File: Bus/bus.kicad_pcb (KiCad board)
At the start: 4 copper layers, 69.3 x 213.7 mm, 38 parts, among them J1 Conn_01x05_Pin, J10 USB_C_Receptacle_PowerOnly_6P, J11 Conn_01x10_Pin, J12 Conn_01x05_Pin, J2 Conn_01x08_Pin, J3 Conn_01x06_Pin, J4 Conn_01x08_Pin, J5 Conn_01x06_Pin, J6 Conn_01x08_Pin, J7 Conn_01x06_Pin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

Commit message: Added pins to bus PCB. Oh boy it's going to be long
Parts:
- added J10: Conn_01x10_Pin, Connector_PinHeader_2.54mm:PinHeader_1x10_P2.54mm_Vertical, F.Cu at (159.8, 28.4)
- added J13: Conn_01x08_Pin, Connector_PinHeader_2.54mm:PinHeader_1x08_P2.54mm_Vertical, F.Cu at (100.3, 173.7)
- added J14: Conn_01x08_Pin, Connector_PinHeader_2.54mm:PinHeader_1x08_P2.54mm_Vertical, F.Cu at (100.6, 196.1)
- added J15: Conn_01x06_Pin, Connector_PinHeader_2.54mm:PinHeader_1x06_P2.54mm_Vertical, F.Cu at (100.6, 48.3)
- added J16: Conn_01x03_Pin, Connector_PinHeader_2.54mm:PinHeader_1x03_P2.54mm_Vertical, F.Cu at (100.6, 65.3)
- added J17: Conn_01x10_Pin, Connector_PinHeader_2.54mm:PinHeader_1x10_P2.54mm_Vertical, F.Cu at (100.6, 75.4)
- added J18: Conn_01x03_Pin, Connector_PinHeader_2.54mm:PinHeader_1x03_P2.54mm_Vertical, F.Cu at (100.7, 102.6)
- added J19: Conn_01x10_Pin, Connector_PinHeader_2.54mm:PinHeader_1x10_P2.54mm_Vertical, F.Cu at (160.3, 241.0)
- added J20: Conn_01x03_Pin, Connector_PinHeader_2.54mm:PinHeader_1x03_P2.54mm_Vertical, F.Cu at (160.5, 268.2)
- added J21: Conn_01x10_Pin, Connector_PinHeader_2.54mm:PinHeader_1x10_P2.54mm_Vertical, F.Cu at (160.3, 200.2)
- added J22: Conn_01x04_Pin, Connector_PinHeader_2.54mm:PinHeader_1x04_P2.54mm_Vertical, F.Cu at (160.3, 227.8)
- J11: value Conn_01x10_Pin -> Conn_01x05_Pin; footprint Connector_PinHeader_2.54mm:PinHeader_1x10_P2.54mm_Vertical -> Connector_PinHeader_2.54mm:PinHeader_1x05_P2.54mm_Vertical
- J12: value Conn_01x05_Pin -> Conn_01x07_Pin; footprint Connector_PinHeader_2.54mm:PinHeader_1x05_P2.54mm_Vertical -> Connector_PinHeader_2.54mm:PinHeader_1x07_P2.54mm_Vertical
- J2, J4, J6: value Conn_01x08_Pin -> Conn_01x10_Pin; footprint Connector_PinHeader_2.54mm:PinHeader_1x08_P2.54mm_Vertical -> Connector_PinHeader_2.54mm:PinHeader_1x10_P2.54mm_Vertical
- J3, J5, J7: value Conn_01x06_Pin -> Conn_01x04_Pin; footprint Connector_PinHeader_2.54mm:PinHeader_1x06_P2.54mm_Vertical -> Connector_PinHeader_2.54mm:PinHeader_1x04_P2.54mm_Vertical
- J9: value Conn_01x06_Pin -> Conn_01x07_Pin; footprint Connector_PinHeader_2.54mm:PinHeader_1x06_P2.54mm_Vertical -> Connector_PinHeader_2.54mm:PinHeader_1x07_P2.54mm_Vertical
- moved J12 128.9 mm to (100.8, 153.2)
- moved J5 77.4 mm to (160.3, 187.7)
- moved J7 77.1 mm to (100.6, 140.0)
- moved J9 55.0 mm to (160.0, 139.2)
- moved J6 51.4 mm to (100.6, 113.3)
- moved J4 48.2 mm to (160.0, 160.0)
- moved J3 39.7 mm to (160.0, 99.6)
- moved J8 28.8 mm to (160.2, 112.0)
- moved J11 22.7 mm to (159.8, 55.9)
- moved J1 13.0 mm to (100.6, 29.0)
- moved J2 10.7 mm to (159.9, 71.9)
- renumbered J10 to J23
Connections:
- J1 pad 4: /~CLK -> /~{CLK}
- J1 pad 5: /Halt -> /HALT
- J11 pad 1: +5V -> /PC_~{JMP}
- J11 pad 2: GND -> /PC_CE
- J11 pad 3: /B7 -> /CLK
- J11 pad 4: /B6 -> /~RST
- J11 pad 5: /B5 -> /PC_~{CO}
- J12 pad 1: /PC ~CO -> +5V
- J12 pad 2: /~RST -> GND
- J12 pad 3: /CLK -> /ALU_CARRY
- J12 pad 4: /PC CE -> /ALU_ZERO
- J12 pad 5: /PC ~JMP -> /~{CLK}
- J2 pad 1: /B7 -> +5V
- J2 pad 2: /B6 -> GND
- J2 pad 3: /B5 -> /B0
- J2 pad 4: /B4 -> /B1
- J2 pad 5: /B3 -> /B2
- J2 pad 6: /B2 -> /B3
- J2 pad 7: /B1 -> /B4
- J2 pad 8: /B0 -> /B5
- J3 pad 1: /ARegister/~Write -> /AR_~{WRITE}
- J3 pad 3: /ARegister/~Read -> /AR_~{READ}
- J4 pad 1: /B7 -> +5V
- J4 pad 2: /B6 -> GND
- J4 pad 3: /B5 -> /B0
- J4 pad 4: /B4 -> /B1
- J4 pad 5: /B3 -> /B2
- J4 pad 6: /B2 -> /B3
- J4 pad 7: /B1 -> /B4
- J4 pad 8: /B0 -> /B5
- J5 pad 3: /BRegister/~Read -> /BR_~{READ}
- J6 pad 1: /B7 -> +5V
- J6 pad 2: /B6 -> GND
- J6 pad 3: /B5 -> /B0
- J6 pad 4: /B4 -> /B1
- J6 pad 5: /InstructionRegister/B3 -> /B2
- J6 pad 6: /InstructionRegister/B2 -> /B3
- J6 pad 7: /InstructionRegister/B1 -> /B4
- J6 pad 8: /InstructionRegister/B0 -> /B5
- J7 pad 1: /InstructionRegister/~Write -> /CLK
- J7 pad 2: /RST -> /IR_~{READ}
- J7 pad 3: /InstructionRegister/~Read -> /RST
- J7 pad 4: /CLK -> /IR_~{WRITE}
- J9 pad 1: /ALU/~Write -> /ALU_~{WRITE}
- J9 pad 2: /ALU/Sub -> /ALU_SUB
- J9 pad 5: /ALU/Carry flag -> /ALU_FI
- J9 pad 6: /ALU/Zero flag -> /ALU_CARRY
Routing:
- net (no net): track 0.00 -> 447.7 mm
- net /PC_~{JMP}: track 0.00 -> 107.8 mm
- net /PC ~CO: track 107.8 -> 0.00 mm
- net /~RST: track 160.5 -> 260.5 mm
- net /PC CE: track 99.9 -> 0.00 mm
- net /PC_~{CO}: track 0.00 -> 97.1 mm
- net /PC ~JMP: track 97.1 -> 0.00 mm
- net /~CLK: track 91.0 -> 0.00 mm, vias 1 -> 0
- net /MAR_~{EN}: track 0.00 -> 91.0 mm, vias 0 -> 1
- net /ARegister/~Write: track 81.2 -> 0.00 mm
- net /Halt: track 76.2 -> 0.00 mm
- net /HALT: track 0.00 -> 76.2 mm
- net /ARegister/~Read: track 75.9 -> 0.00 mm
- net /InstructionRegister/~Write: track 62.7 -> 0.00 mm
- net /InstructionRegister/~Read: track 57.4 -> 0.00 mm
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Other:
- board size 69.3 x 213.7 mm -> 69.3 x 273.9 mm

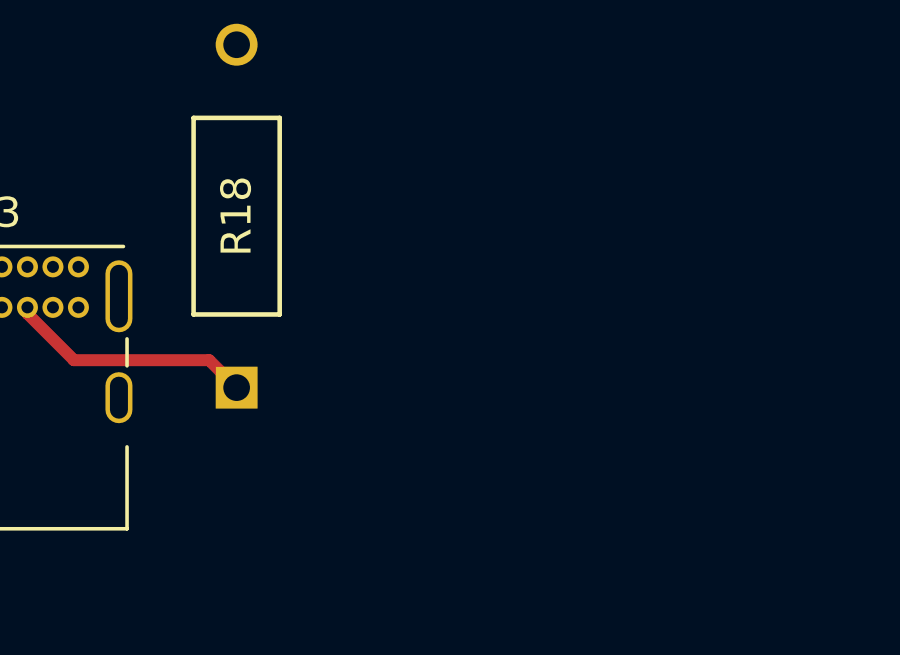
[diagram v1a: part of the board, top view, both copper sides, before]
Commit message: Added an extra power option if I can't solder the USB header
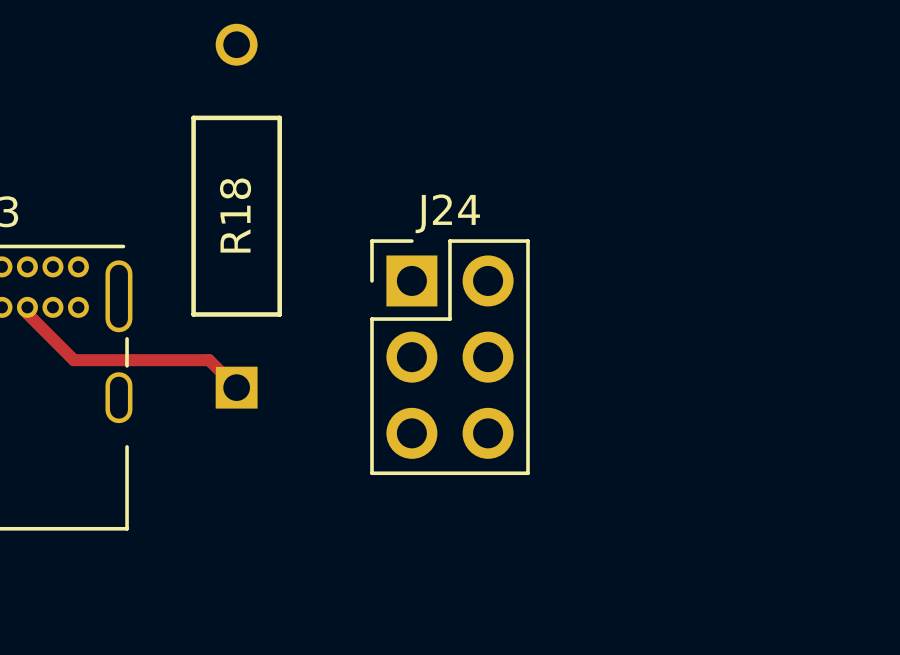
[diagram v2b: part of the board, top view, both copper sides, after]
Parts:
- added J24: Conn_02x03_Counter_Clockwise, Connector_PinHeader_2.54mm:PinHeader_2x03_P2.54mm_Vertical, F.Cu at (139.2, 184.7)

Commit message: Aligned bus pins with where they will fit when connected to the other modules
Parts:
- moved R17 85.7 mm to (109.2, 262.1), turned to 90 degrees
- moved J23 82.5 mm to (107.8, 265.4)
- moved J24 81.6 mm to (118.9, 263.7)
- moved R1 81.1 mm to (120.7, 243.8)
- moved R3 81.1 mm to (127.3, 243.8)
- moved R4 81.1 mm to (130.6, 243.8)
- moved R5 81.1 mm to (133.9, 243.8)
- moved R8 81.1 mm to (143.8, 243.8)
- moved R2 81.1 mm to (124.0, 243.8)
- moved R6 81.1 mm to (137.2, 243.8)
- moved R7 81.1 mm to (140.5, 243.8)
- moved R18 76.8 mm to (112.5, 262.1)
- moved J12 52.3 mm to (100.0, 205.5)
- moved J13 50.8 mm to (100.0, 224.5)
- moved J14 50.2 mm to (100.0, 246.2)
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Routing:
- net /B0: track 260.4 -> 232.7 mm
- net /B7: track 310.7 -> 289.5 mm
- net /B1: track 261.6 -> 241.6 mm
- net /B6: track 299.7 -> 279.8 mm
- net /B5: track 293.3 -> 281.1 mm
- net /B2: track 261.8 -> 250.0 mm
- net Net-(J23-CC1): track 10.4 -> 3.36 mm
- net /B4: track 287.6 -> 281.8 mm
- net /B3: track 262.5 -> 256.9 mm
- net Net-(J23-CC2): track 8.20 -> 11.6 mm
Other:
- board size 69.3 x 273.9 mm -> 69.3 x 281.5 mm

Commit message: Bus fully routed. Minor edits to control to match bus
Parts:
- moved J20 6.43 mm to (156.2, 262.4), turned to 180 degrees
- moved R7 6.14 mm to (146.1, 246.4)
- moved R3 6.14 mm to (132.8, 246.4)
- moved R1 6.14 mm to (126.2, 246.4)
- moved R2 6.14 mm to (129.5, 246.4)
- moved R4 6.14 mm to (136.1, 246.4)
- moved R5 6.14 mm to (139.4, 246.4)
- moved R6 6.14 mm to (142.7, 246.4)
- moved R8 6.14 mm to (149.4, 246.4)
- moved D2 4.58 mm to (141.0, 17.0)
- moved D4 4.58 mm to (127.8, 17.0)
- moved D5 4.58 mm to (121.2, 17.0)
- moved D6 4.58 mm to (114.6, 17.0)
- moved D7 4.58 mm to (108.0, 17.0)
- moved D8 4.58 mm to (101.3, 17.0)
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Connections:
- J13 pad 1: /RAM_~{WO} -> /IR_~{WRITE}
- J13 pad 2: /RAM_RI -> /IR_~{READ}
- J13 pad 3: /IR_~{WRITE} -> /RAM_RI
- J13 pad 4: /IR_~{READ} -> /RAM_~{WO}
- J13 pad 7: /PC_~{CO} -> /PC_~{JMP}
- J14 pad 1: /PC_~{JMP} -> /PC_~{CO}
- J14 pad 2: /AR_~{READ} -> /AR_~{WRITE}
- J14 pad 3: /AR_~{WRITE} -> /AR_~{READ}
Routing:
- net (no net): track 447.7 -> 0.00 mm
- net /~{CLK}: track 0.00 -> 286.2 mm, vias 0 -> 3
- net /PC_CE: track 0.00 -> 250.8 mm, vias 0 -> 1
- net /B0: track 232.7 -> 482.9 mm, vias 4 -> 8
- net /CLK: track 240.8 -> 489.8 mm, vias 6 -> 9
- net /B1: track 241.6 -> 482.8 mm, vias 4 -> 8
- net /B2: track 250.0 -> 482.7 mm, vias 4 -> 8
- net /B3: track 256.9 -> 485.6 mm, vias 4 -> 8
- net /AR_~{WRITE}: track 0.00 -> 215.6 mm, vias 0 -> 1
- net /AR_~{READ}: track 0.00 -> 212.6 mm, vias 0 -> 1
- net /RST: track 142.3 -> 344.4 mm, vias 3 -> 6
- net /B6: track 279.8 -> 478.9 mm, vias 4 -> 7
- net /B7: track 289.5 -> 487.9 mm, vias 4 -> 7
- net /B5: track 281.1 -> 470.3 mm, vias 4 -> 7
- net /B4: track 281.8 -> 464.5 mm, vias 4 -> 7
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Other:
- board size 69.3 x 281.5 mm -> 65.3 x 281.5 mm

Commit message: Bus silkscreen added to all pins
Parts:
- added REF**: MountingHole_2.2mm_M2, MountingHole:MountingHole_2.2mm_M2, F.Cu at (121.8, 45.5)
- added REF**: MountingHole_2.2mm_M2, MountingHole:MountingHole_2.2mm_M2, F.Cu at (178.0, 45.5)
- added REF**: MountingHole_2.2mm_M2, MountingHole:MountingHole_2.2mm_M2, F.Cu at (177.9, 316.2)
- added REF**: MountingHole_2.2mm_M2, MountingHole:MountingHole_2.2mm_M2, F.Cu at (121.8, 316.3)
- moved R10 54.2 mm to (173.1, 57.7), turned to 180 degrees
- moved J20 54.0 mm to (177.9, 311.8)
- moved R14 53.5 mm to (145.4, 57.7), turned to 180 degrees
- moved R9 53.5 mm to (173.1, 61.0), turned to 180 degrees
- moved R13 52.9 mm to (145.4, 61.0), turned to 180 degrees
- moved J23 52.3 mm to (129.5, 313.0)
- moved J24 52.3 mm to (140.8, 311.1)
- moved J6 52.2 mm to (121.7, 201.2)
- moved J4 52.2 mm to (177.9, 215.1)
- moved J9 52.2 mm to (177.9, 183.1)
- moved D2 52.2 mm to (162.7, 64.5)
- moved D5 52.2 mm to (142.9, 64.5)
- moved D7 52.2 mm to (129.7, 64.5)
- moved D8 52.2 mm to (123.1, 64.5)
- moved J1 52.2 mm to (121.7, 72.5)
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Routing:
- net Net-(D2-K): track 3.05 -> 13.3 mm
- net Net-(D6-K): track 3.04 -> 12.0 mm
- net Net-(D7-K): track 3.05 -> 12.0 mm
- net Net-(D3-K): track 3.04 -> 10.7 mm
- net Net-(D1-K): track 3.05 -> 5.28 mm
- net /~{CLK}: track 286.2 -> 288.1 mm
- net /~RST: track 348.1 -> 350.0 mm
- net /B2: track 482.7 -> 484.4 mm
- net /B1: track 482.8 -> 484.5 mm
- net Net-(D8-K): track 3.04 -> 4.61 mm
- net Net-(D5-K): track 3.04 -> 4.61 mm
- net /B0: track 482.9 -> 484.5 mm
- net Net-(D4-K): track 3.04 -> 4.08 mm
- net Net-(J23-CC1): track 4.01 -> 5.03 mm
- net /CLK: track 489.8 -> 489.0 mm
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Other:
- board size 65.3 x 281.5 mm -> 62.2 x 276.8 mm
- board text added: "2C"
- board text added: "A ~{RI}"
- board text added: "A ~{WO}"
- board text added: "ALU CARRY"
- board text added: "ALU FI"
- board text added: "ALU SUB"
- board text added: "ALU ZERO"
- board text added: "ALU ~{WO}"
- board text added: "B ~{RI}"
- board text added: "B0"
- board text added: "B1"
- board text added: "B2"
- board text added: "B3"
- board text added: "B4"
- board text added: "B5"
- board text added: "B6"
- board text added: "B7"
- board text added: "BUS"
- board text added: "CE"
- board text added: "CLK"
- board text added: "CLK HALT"
- board text added: "Carry"
- board text added: "FI"
- board text added: "GND"
- board text added: "Halt"
- board text added: "I ~{RI}"
- board text added: "I ~{WO}"
- board text added: "MAR ~{EN}"
- board text added: "OUT EN"
- board text added: "PC EN"
- board text added: "PC ~{CO}"
- board text added: "PC ~{JMP}"
- board text added: "RAM RI"
- board text added: "RAM ~{WO}"
- board text added: "RI"
- board text added: "RST"
- board text added: "Sub"
- board text added: "VCC"
- board text added: "Zero"
- board text added: "~{CLK}"
- board text added: "~{CO}"
- board text added: "~{EN}"
- board text added: "~{JMP}"
- board text added: "~{RI}"
- board text added: "~{RO}"
- board text added: "~{RST}"
- board text added: "~{WO}"
- board text added: "~{Write}"

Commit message: Final bus silkscreen updates
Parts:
- moved REF** 2.75 mm to (121.8, 48.2)
- moved REF** 2.75 mm to (178.0, 48.2)
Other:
- board size 62.2 x 276.8 mm -> 62.2 x 274.1 mm
- board text added: "A Register"
- board text added: "Arithmethic Logic Unit"
- board text added: "B Register"
- board text added: "Clock"
- board text added: "Control"
- board text added: "Instruction Register"
- board text added: "Memory Access Register"
- board text added: "Output"
- board text added: "Program Counter"
- board text added: "Random Access Memory"
- board text added: "Spare"
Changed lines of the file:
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@@
 	(footprint "MountingHole:MountingHole_2.2mm_M2"
 		(layer "F.Cu")
-		(at 121.793 45.466 90)
+		(at 121.769 48.212 90)
 		(descr "Mounting Hole 2.2mm, no annular, M2")
 		(tags "mounting hole 2.2mm no annular m2")
@@
 		)
 		(fp_line
-			(start -1.62 6)
-			(end -1.62 8.73)
-			(stroke
-				(width 0.12)
-				(type solid)
-			)
-			(layer "F.SilkS")
-		)
-		(fp_line
-			(start -1.62 8.73)
-			(end 7.57 8.73)
-			(stroke
-				(width 0.12)
-				(type solid)
-			)
-			(layer "F.SilkS")
-		)
-		(fp_line
 			(start -1.5 -0.68)
 			(end 7.45 -0.68)
@@
 		)
 		(fp_line
-			(start 7.57 6)
-			(end 7.57 8.73)
-			(stroke
-				(width 0.12)
-				(type solid)
-			)
-			(layer "F.SilkS")
-		)
-		(fp_line
 			(start -2.3 -1.06)
 			(end -2.3 9.11)
@@
 	(footprint "MountingHole:MountingHole_2.2mm_M2"
 		(layer "F.Cu")
-		(at 177.975 45.466)
+		(at 177.951 48.212)
 		(descr "Mounting Hole 2.2mm, no annular, M2")
 		(tags "mounting hole 2.2mm no annular m2")
@@
 	(gr_line
 		(start 118.793 316.278)
-		(end 118.793 45.466)
+		(end 118.769 48.212)
 		(stroke
 			(width 0.05)
@@
 	)
 	(gr_arc
-		(start 177.975 42.466)
-		(mid 180.096321 43.344679)
-		(end 180.975 45.466)
+		(start 177.951 45.212)
+		(mid 180.072321 46.090679)
+		(end 180.951 48.212)
 		(stroke
 			(width 0.05)
@@
 	)
 	(gr_line
-		(start 180.975 45.466)
+		(start 180.951 48.212)
 		(end 180.927001 316.230001)
 		(stroke
@@
 	)
 	(gr_arc
-		(start 118.793 45.466)
-		(mid 119.67168 43.34468)
-		(end 121.793 42.466)
+		(start 118.769 48.212)
+		(mid 119.64768 46.09068)
+		(end 121.769 45.212)
 		(stroke
 			(width 0.05)
@@
 	)
 	(gr_line
-		(start 121.793 42.466)
-		(end 177.975 42.466)
+		(start 121.769 45.212)
+		(end 177.951 45.212)
 		(stroke
 			(width 0.05)
@@
 		)
 	)
+	(gr_text "B\nRegister"
+		(at 163.576 230.124 0)
+		(layer "F.SilkS")
+		(effects
+			(font
+				(size 3 3)
+				(thickness 0.3)
+			)
+		)
+	)
+	(gr_text "Arithmethic\nLogic\nUnit"
+		(at 172.72 172.72 0)
+		(layer "F.SilkS")
+		(effects
+			(font
+				(size 3 3)
+				(thickness 0.3)
+			)
+			(justify right)
+		)
+	)
 	(gr_text "CE"
 		(at 176.276 93.047 0)
@@
 		)
 	)
+	(gr_text "Random\nAccess\nMemory"
+		(at 127.508 155.956 0)
+		(layer "F.SilkS")
+		(effects
+			(font
+				(size 3 3)
+				(thickness 0.3)
+			)
+			(justify left)
+		)
+	)
+	(gr_text "Spare"
+		(at 157.988 309.88 0)
+		(layer "F.SilkS")
+		(effects
+			(font
+				(size 3 3)
+				(thickness 0.3)
+			)
+		)
+	)
 	(gr_text "B1"
 		(at 176.3649 287.4834 0)
@@
 		)
 	)
+	(gr_text "Control"
+		(at 127.508 268.224 0)
+		(layer "F.SilkS")
+		(effects
+			(font
+				(size 3 3)
+				(thickness 0.3)
+			)
+			(justify left)
+		)
+	)
 	(gr_text "~{RST}"
 		(at 122.936 266.319 0)
@@
 		)
 	)
+	(gr_text "Program\nCounter"
+		(at 172.72 77.724 0)
+		(layer "F.SilkS")
+		(effects
+			(font
+				(size 3 3)
+				(thickness 0.3)
+			)
+			(justify right)
+		)
+	)
 	(gr_text "B1"
 		(at 176.53 223.934 0)
@@
 	)
 	(gr_text "I ~{WO}"
-		(at 122.936 272.669 0)
+		(at 123.444 273.268 0)
 		(layer "F.SilkS")
 		(effects
@@
 		)
 	)
+	(gr_text "Output"
+		(at 172.72 281.432 0)
+		(layer "F.SilkS")
+		(effects
+			(font
+				(size 3 3)
+				(thickness 0.3)
+			)
+			(justify right)
+		)
+	)
 	(gr_text "GND"
 		(at 168.499 314.9 90)
@@
 		)
 	)
+	(gr_text "Instruction\nRegister"
+		(at 127.508 216.916 0)
+		(layer "F.SilkS")
+		(effects
+			(font
+				(size 3 3)
+				(thickness 0.3)
+			)
+			(justify left)
+		)
+	)
 	(gr_text "GND"
 		(at 128.11 145.462 0)
@@
 	)
 	(gr_text "BUS"
-		(at 149.86 54.483 0)
+		(at 149.86 55.88 0)
 		(layer "F.SilkS")
 		(effects
@@
 	)
 	(gr_text "I ~{RI}"
-		(at 122.936 274.955 0)
+		(at 123.444 275.554 0)
 		(layer "F.SilkS")
 		(effects
@@
 		)
 	)
+	(gr_text "Memory\nAccess\nRegister"
+		(at 127.508 110.744 0)
+		(layer "F.SilkS")
+		(effects
+			(font
+				(size 3 3)
+				(thickness 0.3)
+			)
+			(justify left)
+		)
+	)
 	(gr_text "GND"
 		(at 176.53 108.807 0)
@@
 		)
 	)
+	(gr_text "Clock"
+		(at 127.508 77.724 0)
+		(layer "F.SilkS")
+		(effects
+			(font
+				(size 3 3)
+				(thickness 0.3)
+			)
+			(justify left)
+		)
+	)
 	(gr_text "VCC"
 		(at 176.28 216.184 0)
@@
 		)
 	)
+	(gr_text "A\nRegister"
+		(at 163.576 120.396 0)
+		(layer "F.SilkS")
+		(effects
+			(font
+				(size 3 3)
+				(thickness 0.3)
+			)
+		)
+	)
